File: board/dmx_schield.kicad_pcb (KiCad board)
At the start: 2 copper layers, 94 x 58.4 mm, 48 parts, among them J1 Screw_Terminal_01x04, J2 Screw_Terminal_01x02, J3 Screw_Terminal_01x03, Q1 BC547/BSR14, SW1 SW_Push, U1 R-78E5.0-0.5, U2 MAX481E, U3 LM75B, U4 74LVC2G34

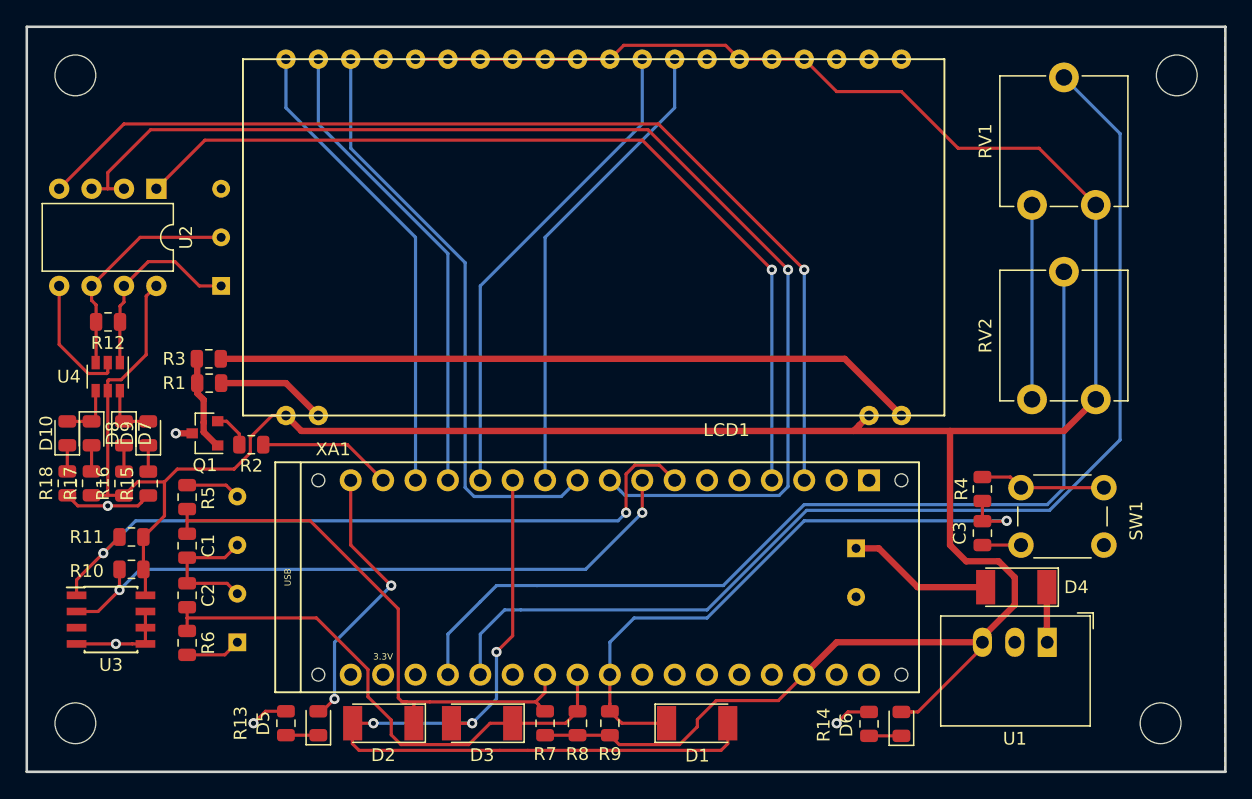
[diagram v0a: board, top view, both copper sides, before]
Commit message: updated board (V1.1), improved readme
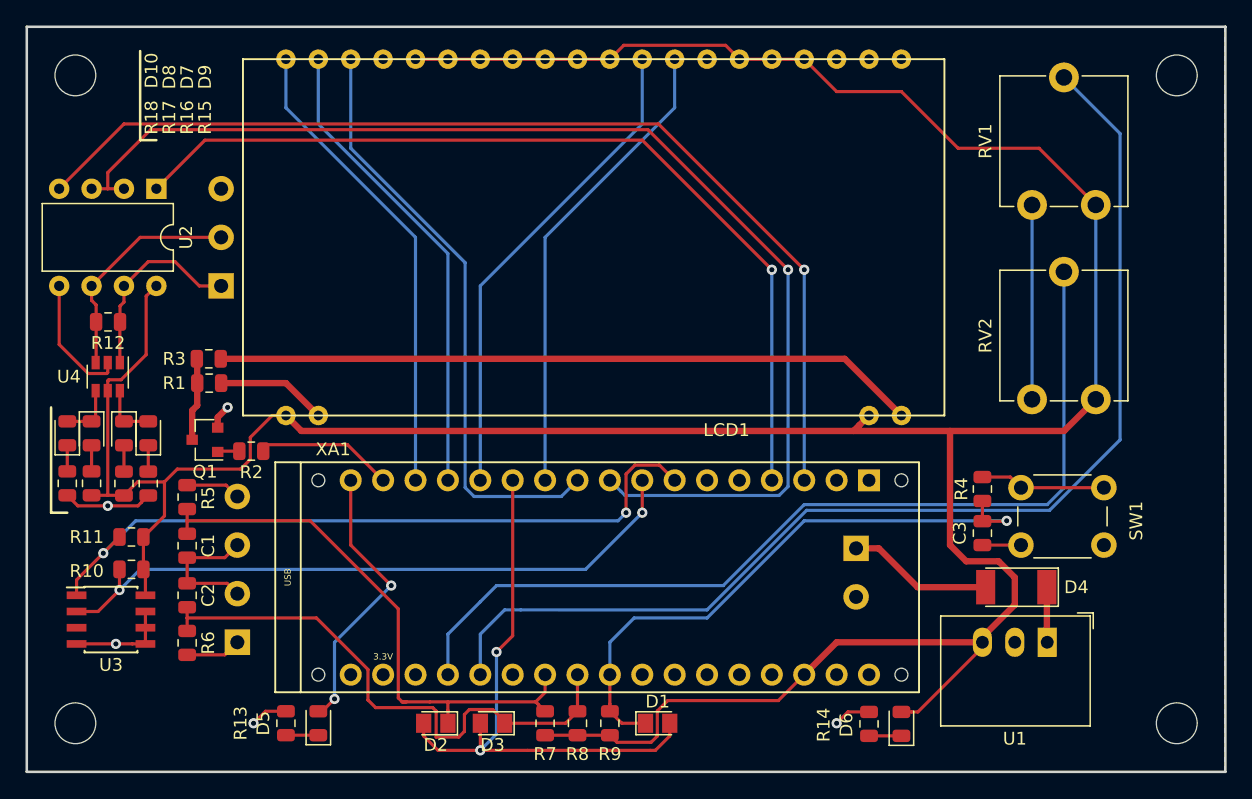
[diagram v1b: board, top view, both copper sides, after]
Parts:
- D1, D2, D3: value LL 5819 -> BAS85; footprint Diode_SMD:D_MELF -> Diode_SMD:D_MicroMELF
- J1: footprint TerminalBlock_MetzConnect:TerminalBlock_MetzConnect_Type086_RT03404HBLC_1x04_P3.81mm_Horizontal -> my_LCD:TerminalBlock_MetzConnect_Type086_RT03404HBLC_1x04_P3.81mm_Horizontal
- J2: footprint TerminalBlock_MetzConnect:TerminalBlock_MetzConnect_Type086_RT03402HBLC_1x02_P3.81mm_Horizontal -> my_LCD:TerminalBlock_MetzConnect_Type086_RT03402HBLC_1x02_P3.81mm_Horizontal
- J3: footprint TerminalBlock_MetzConnect:TerminalBlock_MetzConnect_Type086_RT03403HBLC_1x03_P3.81mm_Horizontal -> my_LCD:TerminalBlock_MetzConnect_Type086_RT03403HBLC_1x03_P3.81mm_Horizontal
- Q1: value BC547/BSR14 -> BSR14
- moved D2 4.12 mm to (110.8, 128.3)
- moved D1 3.10 mm to (128.2, 128.3)
- moved H4 1.27 mm to (168.9, 128.3)
- moved D3 0.81 mm to (115.3, 128.3)
- moved Q1 0.51 mm to (92.7, 106.0)
- moved R2 0.51 mm to (96.3, 106.9)
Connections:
- Q1 pad 2: Net-(Q1-Pad2) -> GND
- Q1 pad 3: GND -> Net-(Q1-Pad3)
- R1 pad 2: Net-(Q1-Pad1) -> Net-(Q1-Pad3)
- R2 pad 2: Net-(Q1-Pad2) -> Net-(Q1-Pad1)
- R3 pad 2: Net-(Q1-Pad1) -> Net-(Q1-Pad3)
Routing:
- net /INTERUPT: track 64.4 -> 46.6 mm, vias 3 -> 2
- net Net-(Q1-Pad3): track 0.00 -> 6.53 mm
- net Net-(Q1-Pad1): track 7.50 -> 1.64 mm
- net Net-(Q1-Pad2): track 2.95 -> 0.00 mm
- net /SW_KW: track 42.5 -> 44.4 mm
- net /SW_COL: track 48.8 -> 47.2 mm
- net VCC: track 256.0 -> 257.0 mm
- net GND: track 61.4 -> 62.0 mm
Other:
- board text added: "1 +24V 2 GND"
- board text added: "GND 3 D+ 2 D- 1"
- board text added: "SW_UP 1 GND 2 GND 3 SW_DOWN 4"
